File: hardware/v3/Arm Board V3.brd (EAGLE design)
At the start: 127 x 76.2 mm, 107 parts, among them CN1 1X4-BIG, IC1 L6208D, IC10 74LVC1G125DCK, IC2 L6208D, IC3 L6208D, IC4 LMV358IDGKR, IC6 ATMEGA16U2-MU, Q2 BC847BSMD, T1 FDN340P, T2 FDN340P, T3 FDN340P, U2 MAX3468CSA, U3 ATSAM3X8EA-AU, Y1 12MHz KX-7 20pF, Y2 32.768Khz, Y4 12MHz KX-7 20pF

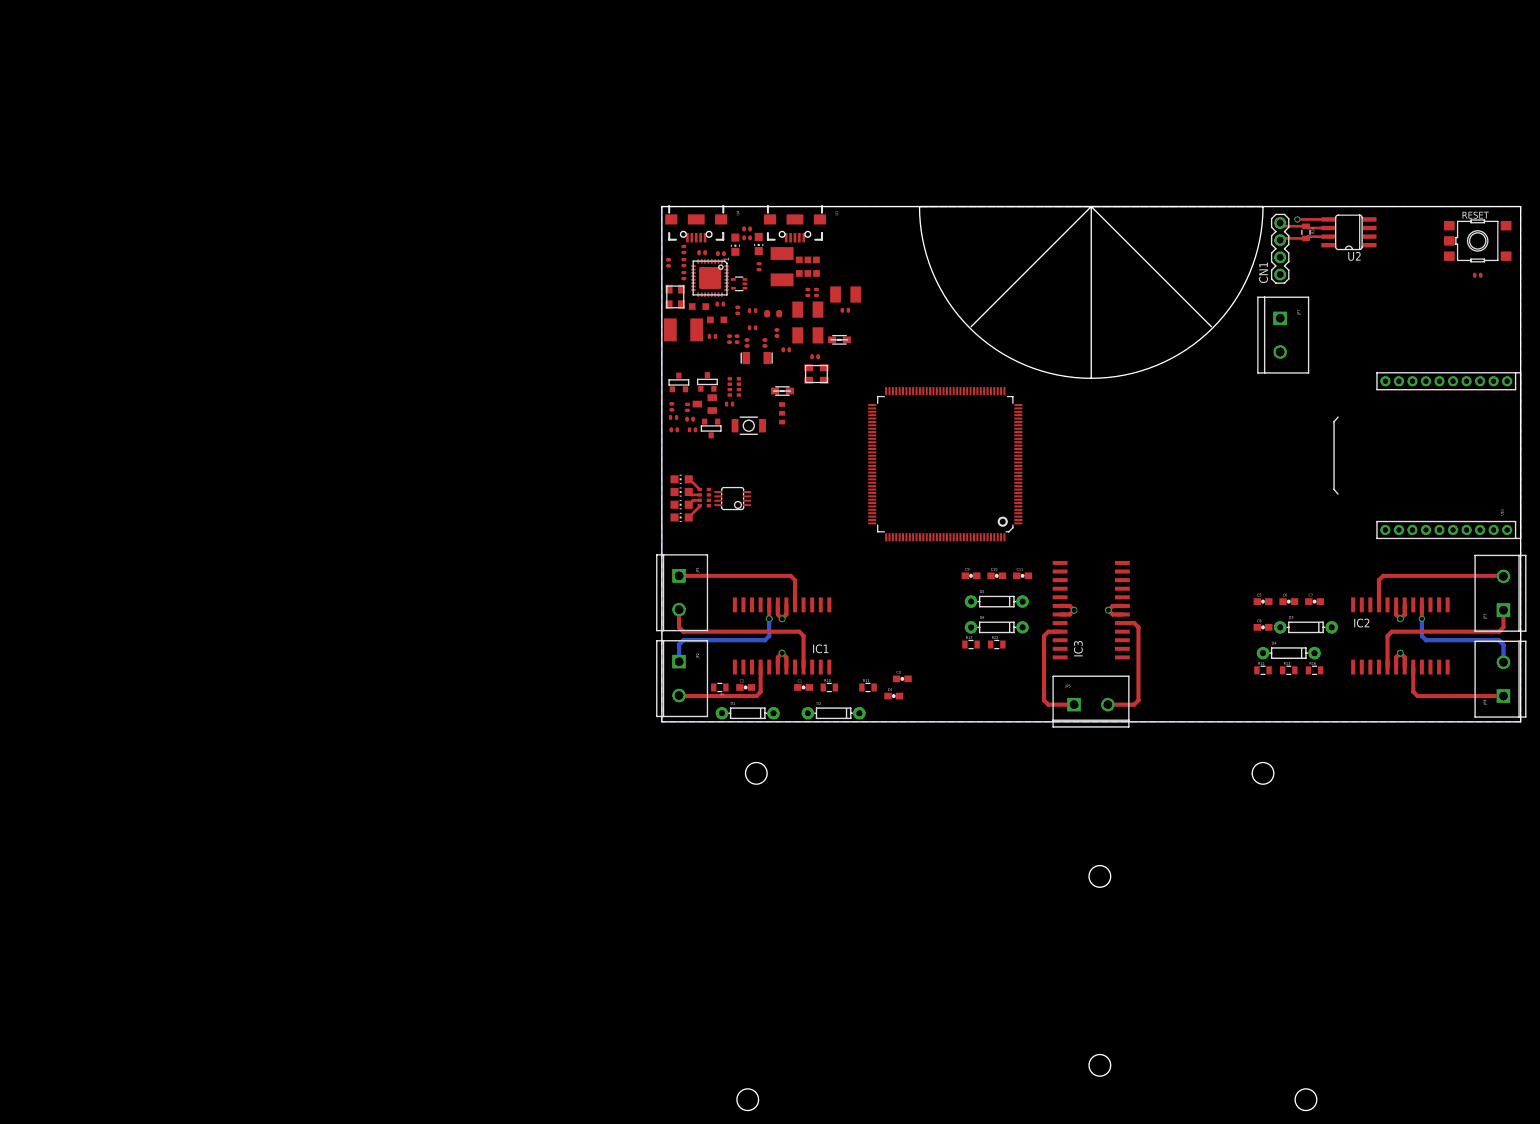
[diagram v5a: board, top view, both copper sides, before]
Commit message: Removed old board file and created a new one
Removed the old board file since there were problems with it from
copying in the Due.  This will also allow us to lay it out logically
with all of the parts on the board.
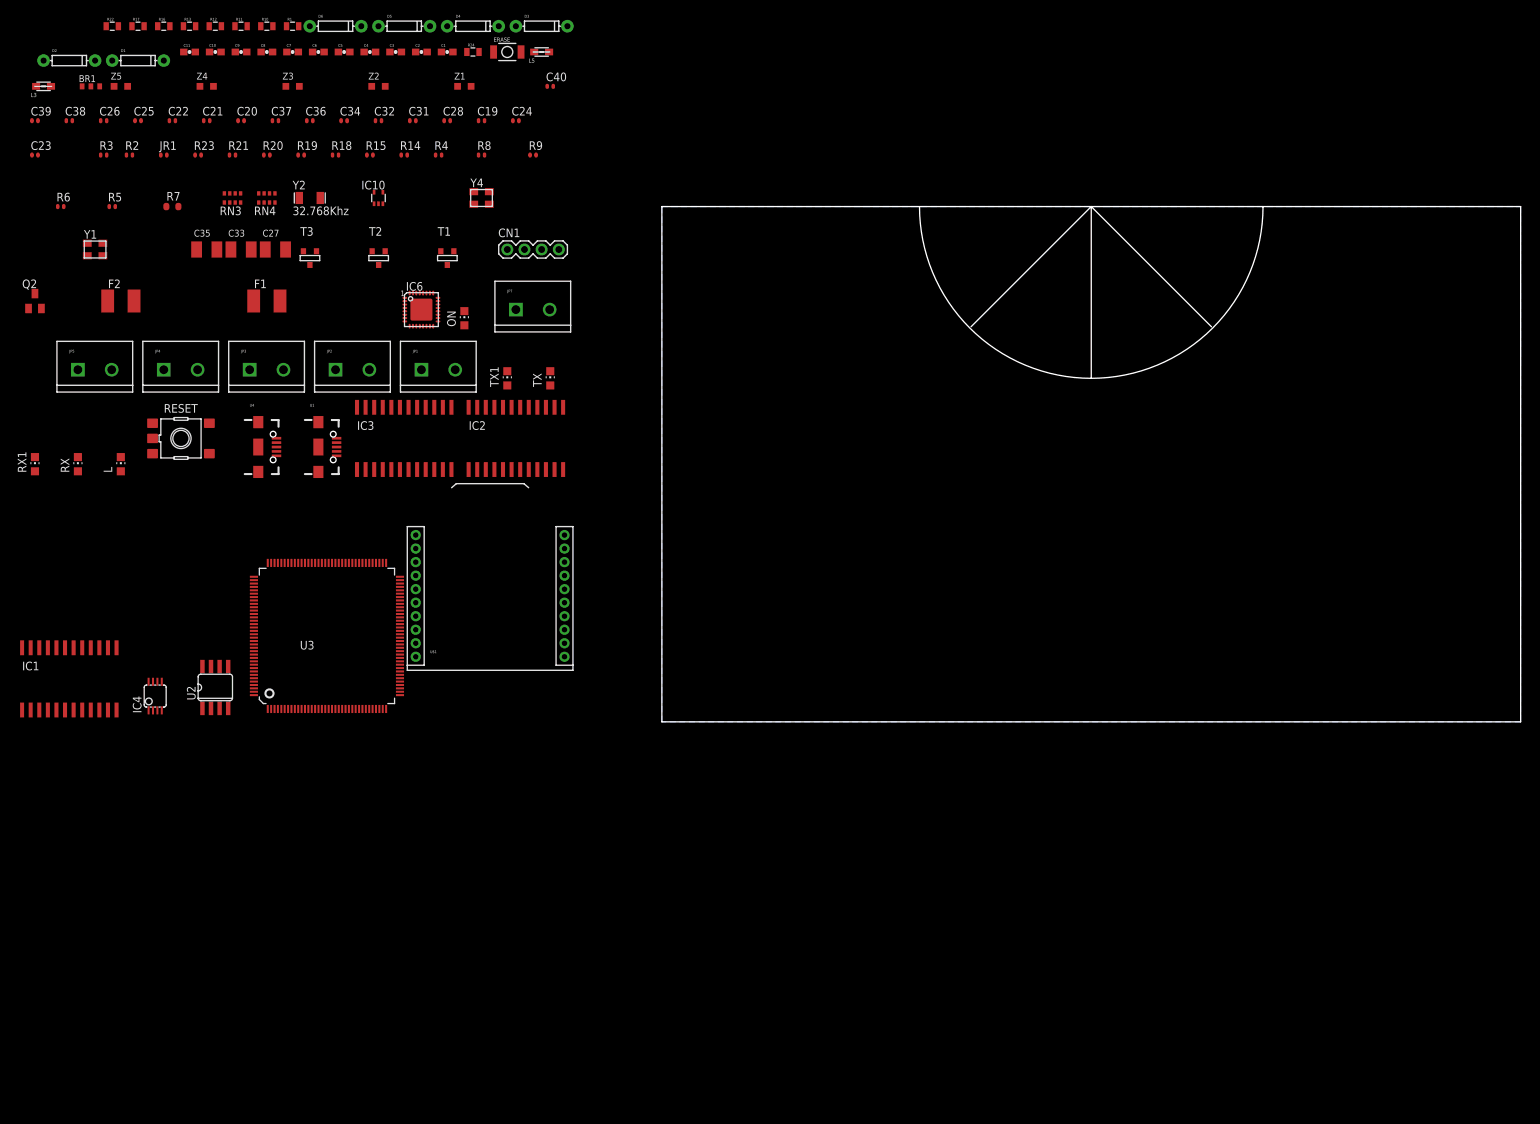
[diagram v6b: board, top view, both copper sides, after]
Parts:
- moved JP4 203.9 mm to (-73.7, 52.1), turned to 0 degrees
- moved R16 195.0 mm to (-73.7, 102.9)
- moved RESET 194.0 mm to (-71.1, 41.9)
- moved JP3 188.8 mm to (-61.0, 52.1), turned to 0 degrees
- moved R13 188.4 mm to (-69.8, 102.9)
- moved C20 184.3 mm to (-62.2, 88.9), turned to 0 degrees
- moved R12 181.9 mm to (-66.0, 102.9)
- moved U2 180.6 mm to (-66.0, 5.08), turned to 0 degrees
- moved C7 171.6 mm to (-54.6, 99.1)
- moved C8 170.1 mm to (-58.4, 99.1)
- moved C6 164.9 mm to (-50.8, 99.1)
- moved R22 159.6 mm to (-81.3, 102.9)
- moved C5 158.3 mm to (-47.0, 99.1)
- moved U$1 155.7 mm to (-25.4, 7.62), turned to 0 degrees
- moved JP5 155.4 mm to (-86.4, 52.1)
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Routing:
- net GND: track 32.4 -> 0.00 mm, vias 7 -> 0
- net A2_1: track 26.2 -> 0.00 mm
- net A1_2: track 24.8 -> 0.00 mm
- net A2_2: track 22.4 -> 0.00 mm
- net A1_1: track 21.1 -> 0.00 mm
- net B1_1: track 21.0 -> 0.00 mm, vias 1 -> 0
- net B2_2: track 19.8 -> 0.00 mm, vias 1 -> 0
- net A1_3: track 18.2 -> 0.00 mm
- net B1_2: track 17.3 -> 0.00 mm
- net A2_3: track 16.9 -> 0.00 mm
- net B2_1: track 16.0 -> 0.00 mm
- net DD-: track 7.39 -> 0.00 mm
- net DD+: track 7.30 -> 0.00 mm
- net N$3: track 2.41 -> 0.00 mm
- net N$54: track 2.25 -> 0.00 mm
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
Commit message: Added Launchpad to Board
This included adding it to the schematic, widening the board, and
placing components.
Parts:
- removed BR1: NM, bibaja:J0402
- removed C19, C28, C31, C32, C34, C36, C37: 100n, SmartPrj:C0402
- removed C20, C26: 10n, SmartPrj:C0402
- removed C21, C22, C25, C39, C40: 22p, SmartPrj:C0402
- removed C23, C24: 22pF_NM, SmartPrj:C0402
- removed C27, C33, C35: 10u, rcl:SMC_B
- removed C38: 1u, SmartPrj:C0402
- removed ERASE: (no value), SmartPrj:SMD_157SW
- removed F1, F2: MF-MSMF050-2 500mA, rcl:L1812
- removed IC10: 74LVC1G125DCK, 74xx-little-us:SC70-5
- removed IC4: LMV358IDGKR, linear:MSOP08
- removed IC6: ATMEGA16U2-MU, SmartPrj:MLF32
- removed JP7: M025MM, SparkFun-Connectors:SCREWTERMINAL-5MM-2
- removed JR1: 0R, SmartPrj:R0402
- removed L, RX, RX1, TX, TX1: YELLOW, led:CHIP-LED0805
- removed L3, L5: MH2029-300Y, wuerth-elektronik:0805
- removed ON: GREEN, led:CHIP-LED0805
- removed Q2: BC847BSMD, transistor-npn:SOT23
- removed R10, R11, R12, R13, R16, R17, R22: (no value), SparkFun-Passives:0805
- removed R14, R15, R21: 1K, SmartPrj:R0402
- removed R18: 10K, SmartPrj:R0402
- removed R19, R20: 22R, SmartPrj:R0402
- removed R23: 1K, Resistenze:R0402
- removed R24: 220, SparkFun-Passives:0805
- removed RESET: TS42, SmartPrj:TS42
- removed RN3: 1k, resistor-dil:CAY16
- removed RN4: 100K, resistor-dil:CAT16
- removed T1, T2, T3: FDN340P, zetex:SOT-23
- removed U2: MAX3468CSA, maxim:SO08
- removed U3: ATSAM3X8EA-AU, SmartPrj:LQFP144
- removed U4: (no value), SparkFun-Connectors:USB-AB-MICRO-SMD_V03
- removed Y1, Y4: 12MHz KX-7 20pF, SmartPrj:CRYSTAL-3.2-2.5
- removed Y2: 32.768Khz, Arduino_Wifi_shield_v018_tG:RESONATOR_EPSON_FC_145
- removed Z1, Z2, Z3, Z4, Z5: CG0603MLC-05E, varistor:CT/CN0603
- added JP6: M025MM, SparkFun-Connectors:SCREWTERMINAL-5MM-2
- added U$2: XBEE-1B2, SparkFun-RF:XBEE-SILK
- R2: value 10K -> (none); device SmartPrj:R0402 -> SparkFun-Passives:0805
- R3: value 1K -> (none); device SmartPrj:R0402 -> SparkFun-Passives:0805
- R4: value 100K -> (none); device SmartPrj:R0402 -> SparkFun-Passives:0805
- R5, R6: value 39R 1% -> (none); device SmartPrj:R0402 -> SparkFun-Passives:0805
- R7: value 6k8 1% -> (none); device SmartPrj:R0603-ROUND -> SparkFun-Passives:0805
- R8: value 0R_NM -> (none); device SmartPrj:R0402 -> SparkFun-Passives:0805
- R9: value 1M_NM -> 220; device SmartPrj:R0402 -> SparkFun-Passives:0805
- U$1: value XBEE-1B2 -> STELLARIS-LAUNCHPADSTELLARIS-LAUNCHPAD-XL; device SparkFun-RF:XBEE-SILK -> StellarisLaunchPad_Fred:LAUNCHPAD-XL
- U1: value (none) -> MAX3468CSA; device SparkFun-Connectors:USB-AB-MICRO-SMD_V03 -> maxim:SO08
- moved R5 238.6 mm to (152.4, 27.9)
- moved R3 237.8 mm to (148.6, 27.9)
- moved JP4 235.1 mm to (156.2, 2.54)
- moved JP5 235.1 mm to (143.5, 2.54)
- moved C7 220.5 mm to (154.9, 30.5)
- moved C5 212.5 mm to (154.9, 33.0)
- moved C6 212.1 mm to (149.9, 30.5)
- moved C4 204.0 mm to (149.9, 33.0)
- moved R4 197.3 mm to (156.2, 27.9)
- moved D4 192.5 mm to (152.4, 35.6)
- moved D2 182.1 mm to (82.5, 33.0)
- moved D3 182.1 mm to (152.4, 38.1)
- moved U1 180.2 mm to (127.0, 69.8)
- moved IC2 175.7 mm to (152.4, 17.8), turned to 270 degrees
- moved R2 173.1 mm to (85.1, 27.9)
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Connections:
- removed net +3V3: BR1.3, C20.2, C37.1, ERASE.1, IC10.5, IC4.6, JR1.1, R4.2, RN3.5, RN3.7, RN3.8, T3.2, U3.105, U3.11, U3.125, U3.52, U3.57, U3.62
- removed net 16U2-TX: IC10.2, IC6.9
- removed net 5-GND: RESET.5
- removed net AD0: U3.78
- removed net AD1: U3.79
- removed net AD10: U3.90
- removed net AD11(TXD3): U3.91
- removed net AD14(RXD3): U3.92
- removed net AD2: U3.80
- removed net AD3: U3.81
- removed net AD4: U3.82
- removed net AD5: U3.83
- removed net AD6: U3.84
- removed net AD7: U3.85
- removed net AD8: U3.88
- removed net AD9: U3.89
- removed net AREF: BR1.1
- removed net AVREF: C19.2, L3.2, U3.75
- removed net AVREFL: BR1.2, C34.2, JR1.2, L3.1
- removed net BD+: R20.2, U4.D+1, Z4.2
- removed net BD-: R19.2, U4.D-1, Z3.2
- removed net CANRX0: U3.24
- removed net CANTX0: U3.23
- removed net CANTX1/IO: U3.140
- removed net CMP: C31.2, IC4.5, Q2.3, RN4.3, RN4.4
- removed net D+: R6.1, U1.D+1, U3.37, Z1.1
- removed net D-: R5.1, U1.D-1, U3.38, Z2.1
- removed net DAC0(CANRX1): U3.76
- removed net DAC1: U3.77
- removed net DTR: IC6.13, R18.1
- removed net EEXTINT: U3.25
- removed net EMDC: U3.123
- removed net EMDIO: U3.127
- removed net ERASE_CMD: IC6.23, T3.3
- removed net ERASE_S: ERASE.2, T3.1, U3.130
- removed net ERXD0: U3.120
- removed net ERXD1: U3.121
- removed net ERX_DV: U3.119
- removed net ERX_ER: U3.122
- removed net ETXD0: U3.115
- removed net ETXD1: U3.118
- removed net ETX_CLK: U3.113
- removed net ETX_EN: U3.114
- removed net GATE_CMD: IC4.7, T1.3
- removed net JTAG_TCK: U3.28
- removed net JTAG_TDI: U3.29
- removed net JTAG_TDO: U3.30
- removed net JTAG_TMS: U3.31
- removed net L13: IC4.1, IC4.2, RN3.6
- removed net MASTER-RESET: C20.1, R23.2, RESET.3, RESET.4, U3.47
- removed net MISO: U3.108
- removed net MOSI: U3.109
- removed net N$1: IC6.26, R21.1
- removed net N$11: R5.2, U3.43
- removed net N$12: R6.2, U3.42
- removed net N$14: R14.2, TX1.A
- removed net N$2: L.A, RN3.3
- removed net N$3: ON.A, RN3.4
- removed net N$4: R15.2, RX1.A
- removed net N$5: R8.2, U3.51
- removed net N$54: RN3.1, RX.A
- removed net N$55: RN3.2, TX.A
- removed net N$6: Q2.1, R3.2, RN4.8
- removed net N$7: R4.1, U3.53
- removed net PIN22: U3.1
- removed net PIN24: U3.8
- removed net PIN31: U3.26
- removed net PIN32: U3.32
- removed net PIN33: U3.55
- removed net PIN34: U3.59
- removed net PIN35: U3.60
- removed net PIN36: U3.116
- removed net PIN37: U3.63
- removed net PIN38: U3.64
- removed net PIN39: U3.65
- removed net PIN40: U3.66
- removed net PIN41: U3.67
- removed net PIN42: U3.71
- removed net PIN43: U3.72
- removed net PIN48: U3.97
- removed net PIN49: U3.96
- removed net PIN50: U3.95
- removed net PIN51: U3.94
- removed net PWM11: U3.20
- removed net PWM12: U3.21
- removed net PWM13: IC4.3, U3.68
- removed net PWM2: U3.144
- removed net PWM3: U3.139
- removed net RD+: IC6.29, R20.1
- removed net RD-: IC6.30, R19.1
- removed net RESET_CMD: IC6.22, R23.1
- removed net RX: IC10.4, U3.27
- removed net RXD0: U3.18
- removed net RXL: RX.C, U3.103
- removed net RXL-U2: IC6.10, RX1.C
- removed net SCL0-3: U3.87
- removed net SCL1: U3.70
- removed net SDA0-3: U3.86
- removed net SDA1: U3.9
- removed net SPCK: U3.110
- removed net SS0/PWM10: U3.102, U3.111
- removed net SS1/PWM4: U3.112, U3.137
- removed net SS3: U3.142
- removed net TX: IC6.8, U3.2
- removed net TXD0: U3.17
- removed net TXL: TX.C, U3.107
- removed net TXL-U2: IC6.11, TX1.C
- removed net UOTGID: U1.ID1, U3.129, Z5.2
- removed net UOTGVBOF: R3.1, U3.128
- removed net USBVCC: C27.+, C35.+, F1.1, R2.2, R21.2, T1.1
- removed net USBVCCU2: C28.1, F2.1, IC6.31, T2.1
- removed net V+: IC4.8
- removed net V-: IC4.4
- removed net VBG: C25.1, R7.2, U3.40
- removed net VDDANA: U3.73
- removed net VDDOUT: L5.1, U3.10, U3.104, U3.124, U3.45, U3.56, U3.61
- removed net VDDOUTMI: U3.41
- removed net VDDPLL: C32.2, C33.+, L5.2, U3.34
- removed net VUCAP: C38.1, IC6.27
- removed net XIN: C22.1, U3.36, Y1.1
- removed net XIN32: C24.1, U3.48, Y2.P$2
- removed net XOUT: C21.1, U3.35, Y1.3
- removed net XOUT32: C23.1, U3.49, Y2.P$1
- removed net XT1: C39.1, IC6.1, R9.1, Y4.1
- removed net XT2: C40.1, IC6.2, R9.2, Y4.3
- removed net XUSB: C26.1, F1.2, U1.VBUS1, U3.39
- removed net XVCC: F2.2, U4.VBUS1
- new net 3.3V: U$1.3.3V
- new net GND2: U$1.GND2
- new net RST: U$1.RST
- new net VBUS: U$1.VBUS
- net +5V: now also U$2.1, U1.8; no longer C36.1, IC6.32, IC6.4, R14.1, R15.1, T1.2, T2.2, U$1.1, U2.8
- net A1_1: now also IC3.5, JP2.1; no longer IC1.5, JP1.1
- net A1_2: now also JP4.1; no longer JP3.1
- net A1_3: now also IC1.5, JP6.2; no longer IC3.5, JP5.2
- net A2_1: now also IC3.21, JP2.2; no longer IC1.21, JP1.2
- net A2_2: now also JP4.2; no longer JP3.2
- net A2_3: now also IC1.21, JP6.1; no longer IC3.21, JP5.1
- net B1_1: now also IC3.8, JP3.1; no longer IC1.8, JP2.1
- net B1_2: now also JP5.1; no longer JP4.1
- net B2_1: now also IC3.16, JP3.2; no longer IC1.16, JP2.2
- net B2_2: now also JP5.2; no longer JP4.2
- net DD+: now also R9.2, U1.7; no longer R24.2, U2.7
- net DD-: now also R9.1, U1.6; no longer R24.1, U2.6
- net GND: now also C11.2, C4.1, C7.2, C8.1, JP1.2, U$2.10, U1.5; no longer C19.1, C2.2, C21.2, C22.2, C23.2, C24.2, C25.2, C26.2, C27.-, C28.2, C31.1, C32.1, C33.-, C34.1, C35.-, C36.2, C37.2, C38.2, C39.2, C40.2, C5.1, C6.2, C9.1, IC10.1, IC10.3, IC6.28, IC6.3, IC6.33, JP7.2, L.C, ON.C, Q2.2, R18.2, R2.1, R7.1, R8.1, RESET.1, RESET.2, RN4.1, RN4.2, RN4.5, RN4.7, T2.3, U$1.10, U1.GND1, U2.5, U3.106, U3.12, U3.126, U3.33, U3.44, U3.46, U3.54, U3.58, U3.74, U4.GND1, Y1.2, Y1.4, Y4.2, Y4.4, Z1.2, Z2.2, Z3.1, Z4.1, Z5.1
- net N$10: now also C5.2, R4.1; no longer C8.2, R16.1
- net N$13: now also C9.1, IC3.22; no longer C4.1, IC1.22
- net N$15: now also C9.2, R7.1; no longer C4.2, R11.1
- net N$16: now also C5.1; no longer C8.1
- net N$17: now also D1.A, D2.C, R2.2; no longer D5.C, D6.A, R22.2
- net N$18: now also C2.2, R2.1; no longer C11.2, R22.1
- net N$19: now also C2.1, IC1.22; no longer C11.1, IC3.22
- net N$8: now also D3.A, D4.C, R4.2; no longer D3.C, D4.A, R16.2
- net N$9: now also D5.A, D6.C, R7.2; no longer D1.C, D2.A, R11.2
- net OCD_A_1: now also C8.2, IC3.23, IC3.4, R6.1; no longer C1.2, IC1.23, IC1.4, R10.1
- net OCD_A_2: now also C4.2, R3.1; no longer C5.2, R13.1
- net OCD_A_3: now also C1.2, IC1.23, IC1.4, R1.1; no longer C9.2, IC3.23, IC3.4, R17.1
- net OCD_B_1: now also C11.1, IC3.14, IC3.9, R8.1; no longer C2.1, IC1.14, IC1.9, R1.1
- net OCD_B_2: now also C7.1, R5.1; no longer C6.1, R12.1
- net PIN23: now also U1.2, U1.3; no longer U2.2, U2.3, U3.7
- net PIN25: no longer U3.13
- net PIN26: no longer U3.14
- net PIN27: no longer U3.15
- net PIN28: no longer U3.16
- net PIN29: now also IC1.1; no longer IC3.1, U3.19
- net PIN30: now also IC1.2; no longer IC3.2, U3.22
- net PIN44: now also IC3.1; no longer IC1.1, U3.101
- net PIN45: now also IC3.2; no longer IC1.2, U3.100
- net PIN46: now also IC3.11; no longer IC1.11, U3.99
- net PIN47: now also IC3.12; no longer IC1.12, U3.98
- net PWM5: now also R3.2; no longer R13.2, U3.136
- net PWM6: now also R5.2; no longer R12.2, U3.135
- net PWM7: now also R1.2; no longer R17.2, U3.134
- net PWM8: now also R6.2; no longer R10.2, U3.133
- net PWM9: now also R8.2; no longer R1.2, U3.132
- net RXD1: now also U1.1; no longer U2.1, U3.5
- net RXD2: now also U$2.2; no longer U$1.2, U3.3
- net TXD1: now also U1.4; no longer U2.4, U3.6
- net TXD2: now also U$2.3; no longer U$1.3, U3.4
- net VBOOT_1: now also C10.2, D5.C, IC3.15; no longer C3.2, D2.C, IC1.15
- net VBOOT_2: now also C6.2, D3.C; no longer C7.2, D4.C
- net VBOOT_3: now also C3.2, D1.C, IC1.15; no longer C10.2, D6.C, IC3.15
- net VIN: now also JP1.1; no longer JP7.1, RN4.6
- net VS: now also C6.1, D2.A, D4.A, D6.A; no longer C7.1, D1.A, D3.A, D5.A
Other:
- board size 127 x 76.2 mm -> 165.1 x 76.2 mm

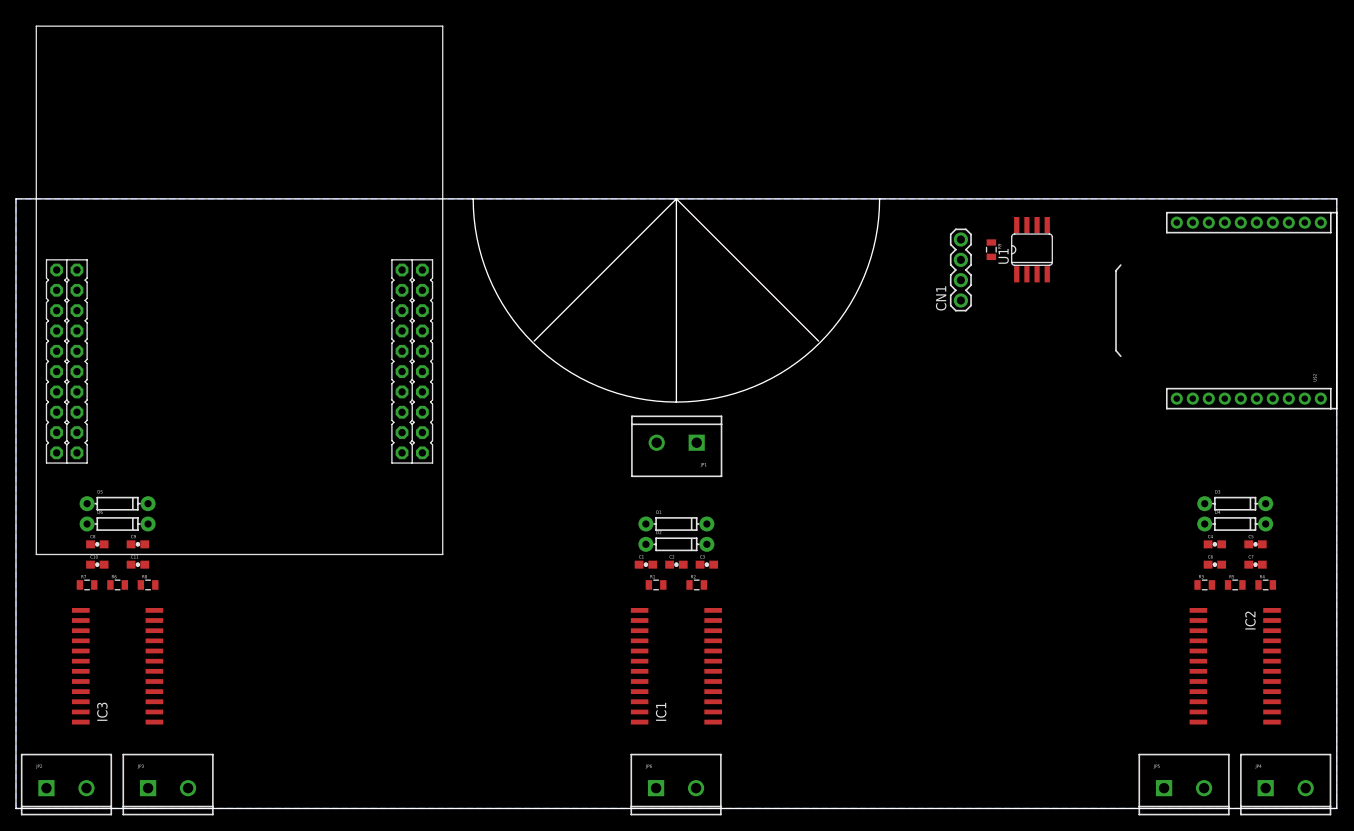
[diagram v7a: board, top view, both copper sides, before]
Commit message: Started routing and added RJ-45
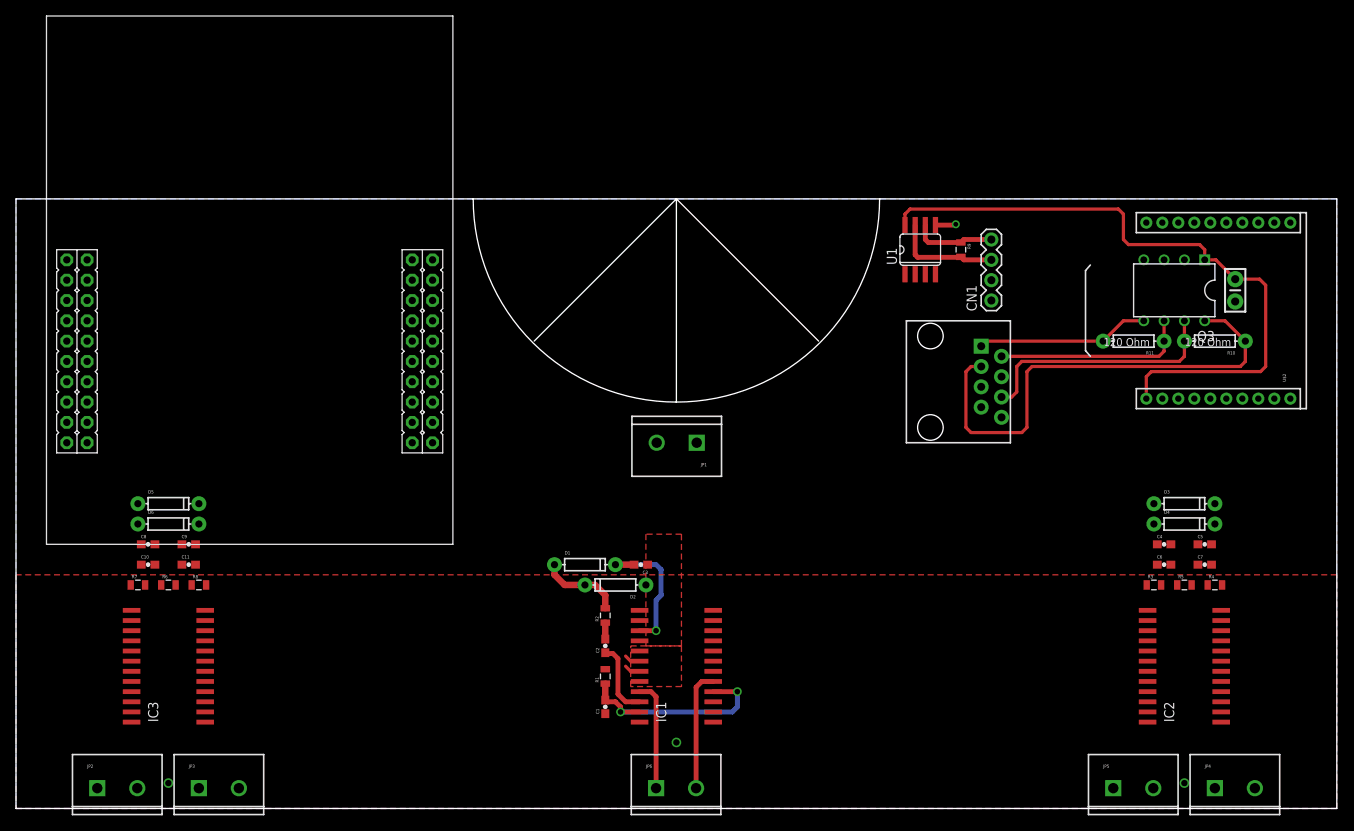
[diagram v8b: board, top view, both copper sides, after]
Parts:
- added C12: .1uF, SparkFun-Capacitors:CAP-PTH-SMALL-KIT
- added Q3: Q_LTC490, PCB0M1:DIP8
- added R10, R11: 120 Ohm, SparkFun-Passives:AXIAL-0.3
- added U$3: RJ45-8PTH, SparkFun-Connectors:RJ45-8
- moved C1 18.5 mm to (73.7, 12.7), turned to 90 degrees
- moved U1 14.0 mm to (113.0, 69.8)
- moved C2 13.5 mm to (73.7, 20.3), turned to 90 degrees
- moved R1 13.1 mm to (73.7, 16.5), turned to 90 degrees
- moved D1 12.5 mm to (71.1, 30.5)
- moved R2 12.0 mm to (73.7, 24.1), turned to 90 degrees
- moved D2 9.16 mm to (74.9, 27.9), turned to 180 degrees
- moved C3 8.25 mm to (78.1, 30.5), turned to 180 degrees
- moved C4 6.35 mm to (143.5, 33.0)
- moved C6 6.35 mm to (143.5, 30.5)
- moved C10 6.35 mm to (16.5, 30.5)
- moved C8 6.35 mm to (16.5, 33.0)
- moved D5 6.35 mm to (19.1, 38.1)
- moved D6 6.35 mm to (19.1, 35.6)
- moved IC3 6.35 mm to (19.1, 17.8)
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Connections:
- net 3.3V renamed +3V3
- new net DM: Q3.3
- new net N$1: Q3.6, R11.P$1, U$3.2
- new net N$2: Q3.7, R10.P$2, U$3.6
- new net N$3: Q3.8, R10.P$1, U$3.3
- new net N$5: Q3.5, R11.P$2, U$3.1
- new net RM: Q3.2
- net +5V: now also C12.1, Q3.1
- net GND: now also C12.2, Q3.4, U$3.7, U$3.8
- net OCD_A_1: no longer IC2.4
- net OCD_A_2: now also IC2.4
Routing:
- net +5V: track 0.00 -> 81.6 mm
- net N$3: track 0.00 -> 60.8 mm
- net N$2: track 0.00 -> 31.3 mm
- net OCD_A_3: track 0.00 -> 27.1 mm, vias 0 -> 2
- net N$1: track 0.00 -> 24.4 mm
- net N$5: track 0.00 -> 21.6 mm
- net VBOOT_3: track 0.00 -> 18.2 mm, vias 0 -> 1
- net A1_3: track 0.00 -> 15.1 mm
- net A2_3: track 0.00 -> 13.8 mm
- net DD+: track 0.00 -> 13.5 mm
- net DD-: track 0.00 -> 10.4 mm
- net N$17: track 0.00 -> 10.3 mm
- net N$19: track 0.00 -> 9.44 mm
- net GND: track 0.00 -> 6.61 mm, vias 0 -> 4
- net N$18: track 0.00 -> 2.06 mm
- added copper zone on layer 1, net GND
- added copper zone on layer 1, net VS
